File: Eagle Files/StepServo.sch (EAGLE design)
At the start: 8 parts, among them J2 1X2-3.5MM

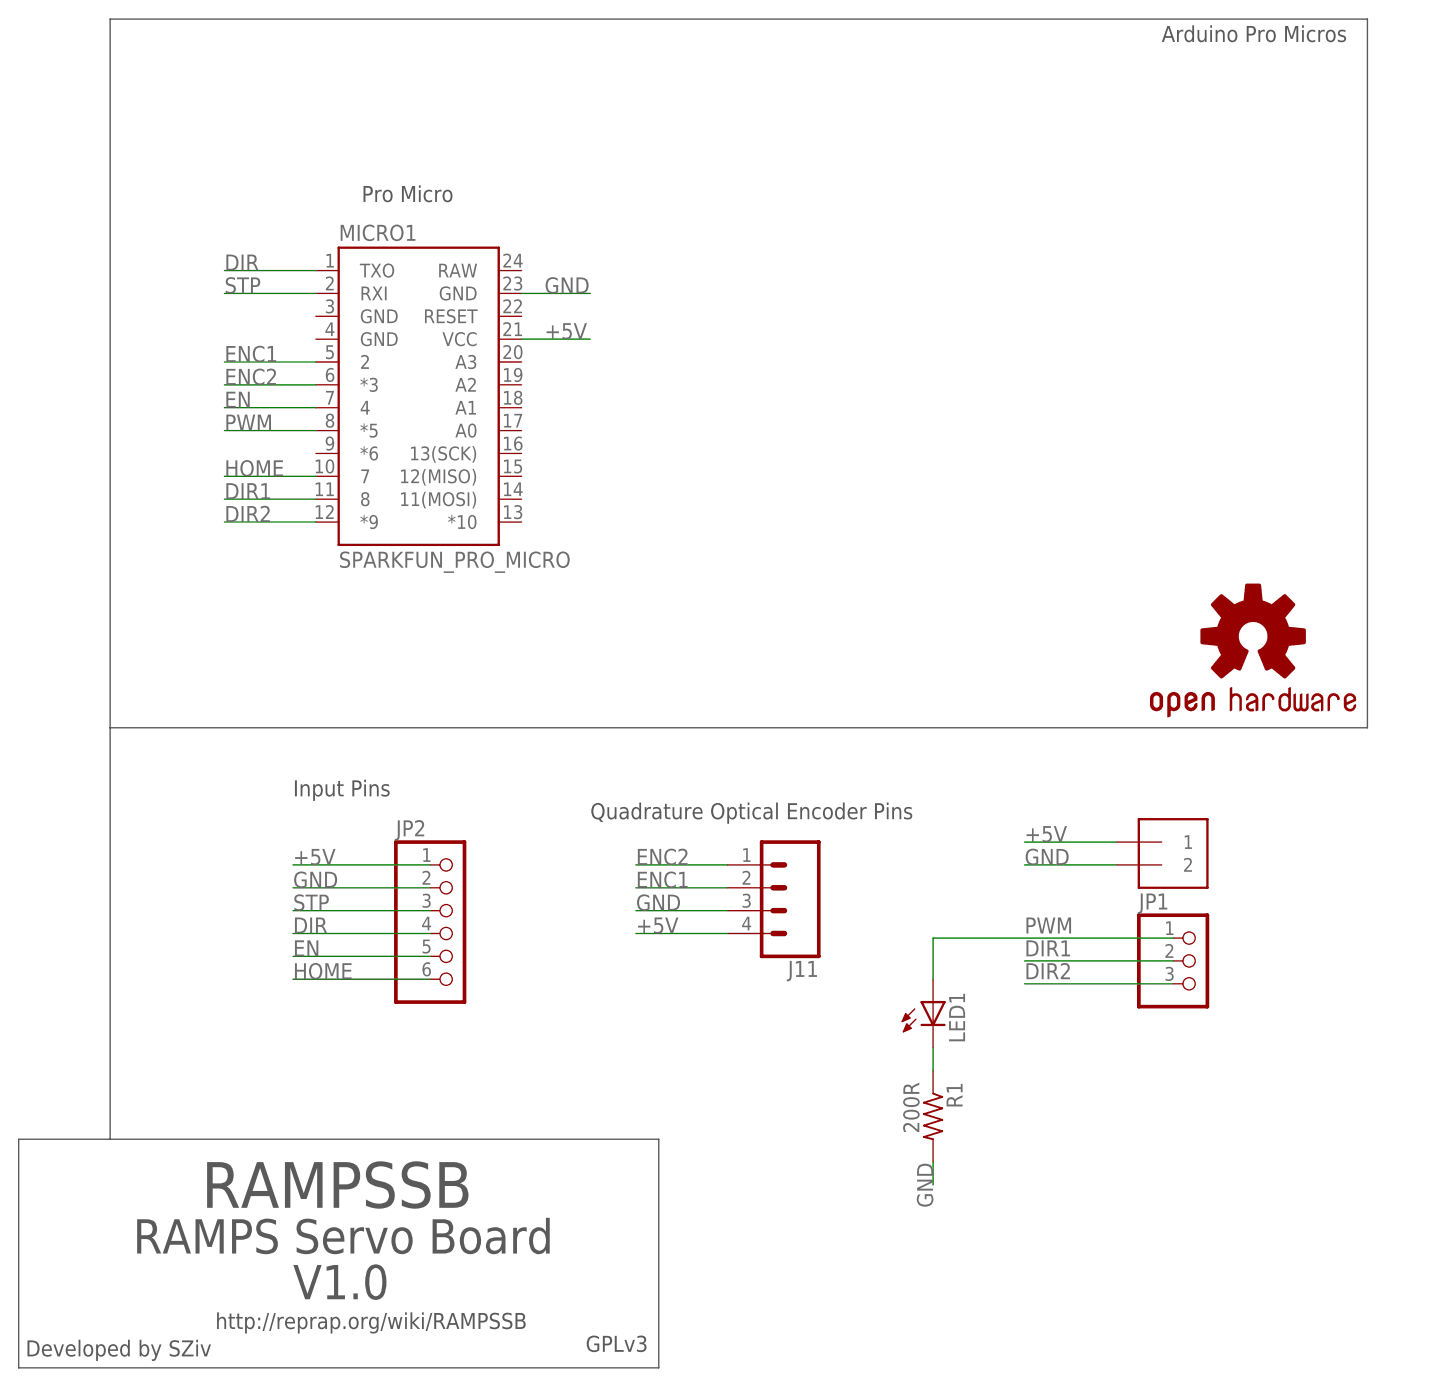
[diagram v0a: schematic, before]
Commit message: Fixed some bad markers on silkscreen, and cleaned up schematic
Fixed some bad markers on silkscreen, and cleaned up schematic
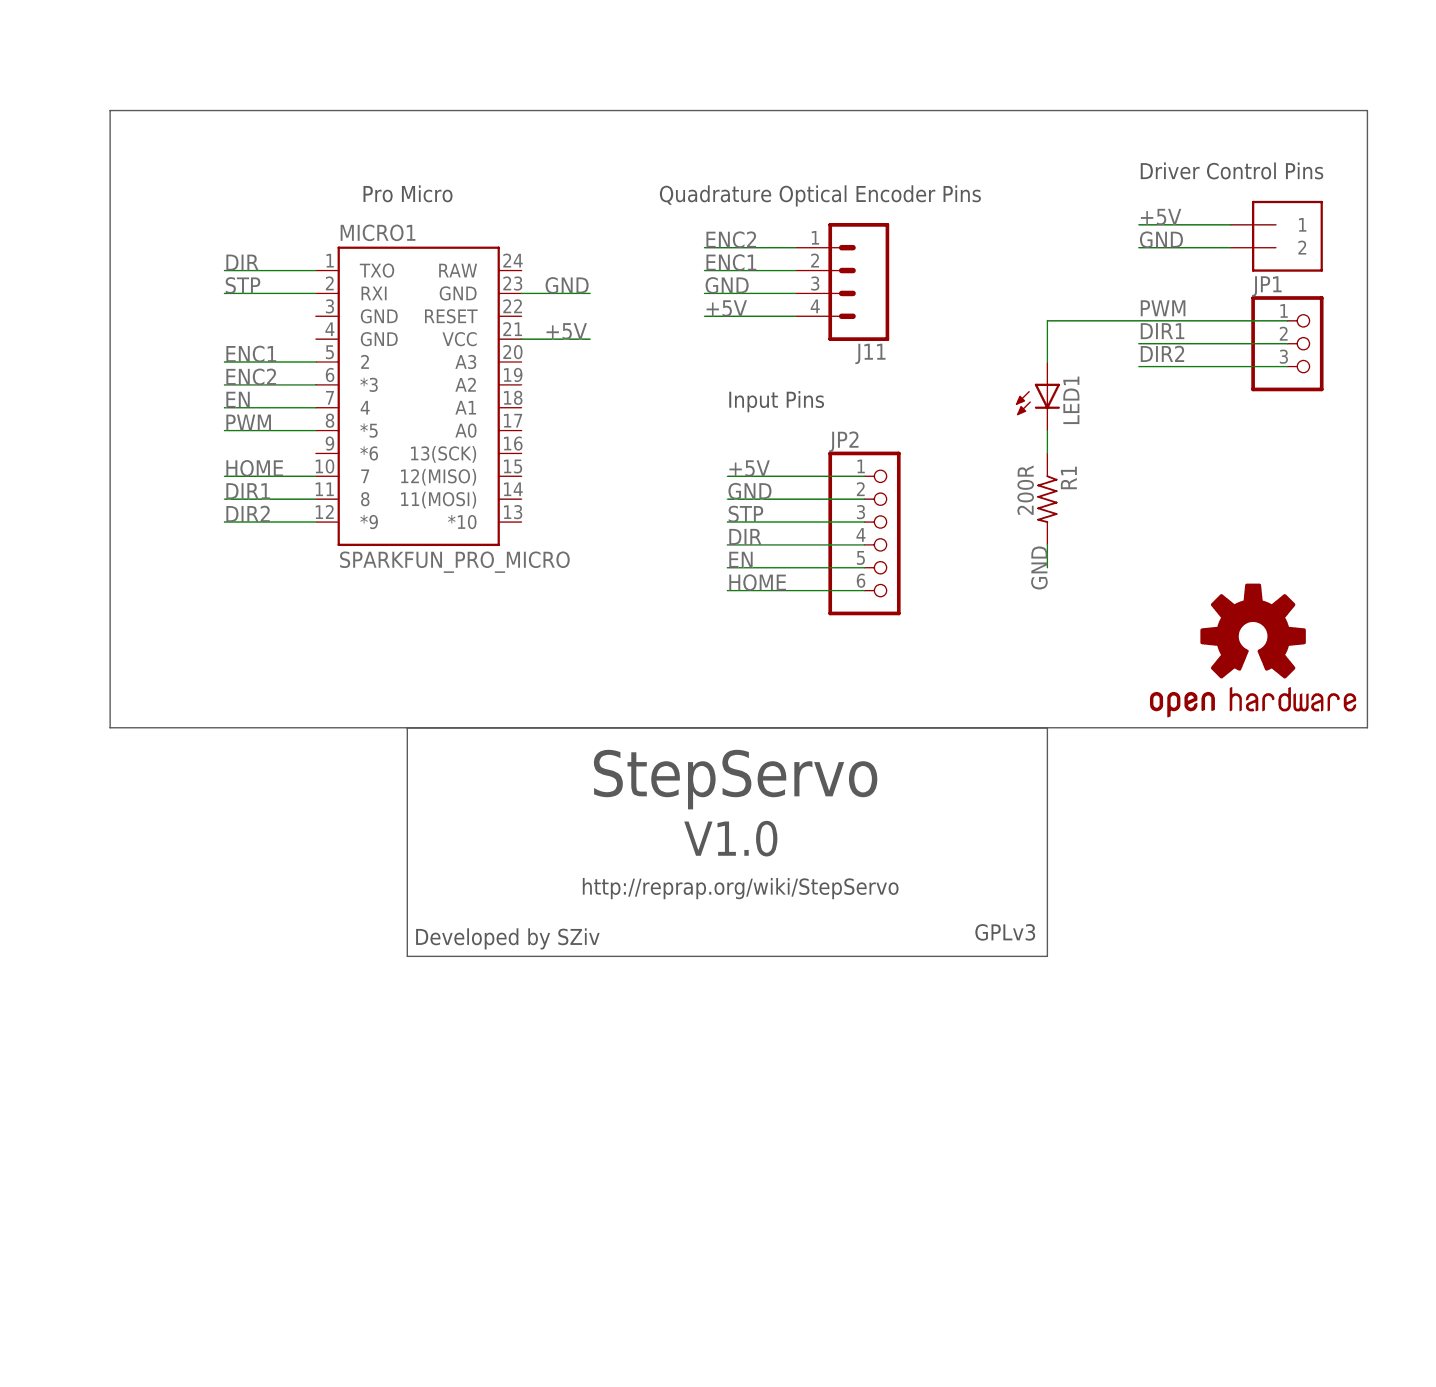
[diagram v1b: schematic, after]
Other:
- note added: "Driver Control Pins"
- note added: "StepServo"
- note added: "http://reprap.org/wiki/StepServo"
- note removed: "Arduino Pro Micros"
- note removed: "RAMPS Servo Board"
- note removed: "RAMPSSB"
- note removed: "http://reprap.org/wiki/RAMPSSB"
- moved on the sheet: J11, JP1, JP2, LED1, R1
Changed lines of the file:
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@@
 <plain>
 <text x="165.354" y="-80.01" size="3.81" layer="97"></text>
-<wire x1="27.94" y1="-12.7" x2="99.06" y2="-12.7" width="0.1524" layer="97"/>
-<wire x1="177.8" y1="58.42" x2="177.8" y2="137.16" width="0.1524" layer="97"/>
-<wire x1="177.8" y1="137.16" x2="38.1" y2="137.16" width="0.1524" layer="97"/>
-<wire x1="38.1" y1="137.16" x2="38.1" y2="58.42" width="0.1524" layer="97"/>
+<wire x1="71.12" y1="33.02" x2="142.24" y2="33.02" width="0.1524" layer="97"/>
+<wire x1="177.8" y1="58.42" x2="177.8" y2="127" width="0.1524" layer="97"/>
+<wire x1="177.8" y1="127" x2="38.1" y2="127" width="0.1524" layer="97"/>
+<wire x1="38.1" y1="127" x2="38.1" y2="58.42" width="0.1524" layer="97"/>
 <wire x1="38.1" y1="58.42" x2="177.8" y2="58.42" width="0.1524" layer="97"/>
-<wire x1="38.1" y1="58.42" x2="38.1" y2="12.7" width="0.1524" layer="97"/>
-<wire x1="38.1" y1="12.7" x2="99.06" y2="12.7" width="0.1524" layer="97"/>
-<wire x1="99.06" y1="12.7" x2="99.06" y2="-12.7" width="0.1524" layer="97"/>
-<wire x1="38.1" y1="12.7" x2="27.94" y2="12.7" width="0.1524" layer="97"/>
-<wire x1="27.94" y1="12.7" x2="27.94" y2="-12.7" width="0.1524" layer="97"/>
-<text x="91.44" y="48.26" size="1.778" layer="97">Quadrature Optical Encoder Pins</text>
-<text x="154.94" y="134.62" size="1.778" layer="97">Arduino Pro Micros</text>
-<text x="48.26" y="5.08" size="5.08" layer="97">RAMPSSB</text>
-<text x="40.64" y="0" size="3.81" layer="97">RAMPS Servo Board</text>
-<text x="58.42" y="-5.08" size="3.81" layer="97">V1.0</text>
-<text x="28.702" y="-11.43" size="1.778" layer="97">Developed by SZiv</text>
-<text x="90.932" y="-10.922" size="1.778" layer="97">GPLv3</text>
-<text x="49.784" y="-8.382" size="1.778" layer="97">http://reprap.org/wiki/RAMPSSB</text>
+<wire x1="71.12" y1="58.42" x2="142.24" y2="58.42" width="0.1524" layer="97"/>
+<wire x1="142.24" y1="58.42" x2="142.24" y2="33.02" width="0.1524" layer="97"/>
+<wire x1="71.12" y1="58.42" x2="71.12" y2="33.02" width="0.1524" layer="97"/>
+<text x="99.06" y="116.84" size="1.778" layer="97">Quadrature Optical Encoder Pins</text>
+<text x="91.44" y="50.8" size="5.08" layer="97">StepServo</text>
+<text x="101.854" y="44.196" size="3.81" layer="97">V1.0</text>
+<text x="71.882" y="34.29" size="1.778" layer="97">Developed by SZiv</text>
+<text x="134.112" y="34.798" size="1.778" layer="97">GPLv3</text>
+<text x="90.424" y="39.878" size="1.778" layer="97">http://reprap.org/wiki/StepServo</text>
 <text x="66.04" y="116.84" size="1.778" layer="97">Pro Micro</text>
-<text x="58.42" y="50.8" size="1.778" layer="97">Input Pins</text>
+<text x="106.68" y="93.98" size="1.778" layer="97">Input Pins</text>
+<text x="152.4" y="119.38" size="1.778" layer="97">Driver Control Pins</text>
 </plain>
 <instances>
-<instance part="J11" gate="G$1" x="111.76" y="40.64" rot="R180"/>
+<instance part="J11" gate="G$1" x="119.38" y="109.22" rot="R180"/>
 <instance part="MICRO1" gate="G$1" x="71.12" y="93.98"/>
 <instance part="LOGO1" gate="G$1" x="165.1" y="68.58"/>
-<instance part="LED1" gate="G$1" x="129.54" y="27.94"/>
-<instance part="R1" gate="G$1" x="129.54" y="15.24" rot="R270"/>
-<instance part="J2" gate="G$1" x="154.94" y="43.18"/>
-<instance part="JP2" gate="A" x="76.2" y="35.56"/>
-<instance part="JP1" gate="A" x="158.75" y="32.512"/>
+<instance part="LED1" gate="G$1" x="142.24" y="96.52"/>
+<instance part="R1" gate="G$1" x="142.24" y="83.82" rot="R270"/>
+<instance part="J2" gate="G$1" x="167.64" y="111.76"/>
+<instance part="JP2" gate="A" x="124.46" y="78.74"/>
+<instance part="JP1" gate="A" x="171.45" y="101.092"/>
 </instances>
 <busses>
@@
 <segment>
 <pinref part="J11" gate="G$1" pin="4"/>
-<wire x1="96.52" y1="35.56" x2="106.68" y2="35.56" width="0.1524" layer="91"/>
-<label x="96.52" y="35.56" size="1.778" layer="95"/>
+<wire x1="104.14" y1="104.14" x2="114.3" y2="104.14" width="0.1524" layer="91"/>
+<label x="104.14" y="104.14" size="1.778" layer="95"/>
 </segment>
 <segment>
@@
 <segment>
 <pinref part="JP2" gate="A" pin="1"/>
-<wire x1="73.66" y1="43.18" x2="58.42" y2="43.18" width="0.1524" layer="91"/>
-<label x="58.42" y="43.18" size="1.778" layer="95"/>
+<wire x1="121.92" y1="86.36" x2="106.68" y2="86.36" width="0.1524" layer="91"/>
+<label x="106.68" y="86.36" size="1.778" layer="95"/>
 </segment>
 <segment>
 <pinref part="J2" gate="G$1" pin="1"/>
-<wire x1="149.86" y1="45.72" x2="139.7" y2="45.72" width="0.1524" layer="91"/>
-<label x="139.7" y="45.72" size="1.778" layer="95"/>
+<wire x1="162.56" y1="114.3" x2="152.4" y2="114.3" width="0.1524" layer="91"/>
+<label x="152.4" y="114.3" size="1.778" layer="95"/>
 </segment>
 </net>
@@
 <segment>
 <pinref part="J11" gate="G$1" pin="3"/>
-<wire x1="96.52" y1="38.1" x2="106.68" y2="38.1" width="0.1524" layer="91"/>
-<label x="96.52" y="38.1" size="1.778" layer="95"/>
+<wire x1="104.14" y1="106.68" x2="114.3" y2="106.68" width="0.1524" layer="91"/>
+<label x="104.14" y="106.68" size="1.778" layer="95"/>
 </segment>
 <segment>
@@
 <segment>
 <pinref part="JP2" gate="A" pin="2"/>
-<wire x1="73.66" y1="40.64" x2="58.42" y2="40.64" width="0.1524" layer="91"/>
-<label x="58.42" y="40.64" size="1.778" layer="95"/>
+<wire x1="121.92" y1="83.82" x2="106.68" y2="83.82" width="0.1524" layer="91"/>
+<label x="106.68" y="83.82" size="1.778" layer="95"/>
 </segment>
 <segment>
 <pinref part="J2" gate="G$1" pin="2"/>
-<wire x1="149.86" y1="43.18" x2="139.7" y2="43.18" width="0.1524" layer="91"/>
-<label x="139.7" y="43.18" size="1.778" layer="95"/>
+<wire x1="162.56" y1="111.76" x2="152.4" y2="111.76" width="0.1524" layer="91"/>
+<label x="152.4" y="111.76" size="1.778" layer="95"/>
 </segment>
 <segment>
 <pinref part="R1" gate="G$1" pin="2"/>
-<wire x1="129.54" y1="10.16" x2="129.54" y2="7.62" width="0.1524" layer="91"/>
-<label x="129.54" y="5.08" size="1.778" layer="95" rot="R90"/>
+<wire x1="142.24" y1="78.74" x2="142.24" y2="76.2" width="0.1524" layer="91"/>
+<label x="142.24" y="73.66" size="1.778" layer="95" rot="R90"/>
 </segment>
 </net>
@@
 <segment>
 <pinref part="JP1" gate="A" pin="2"/>
-<wire x1="156.21" y1="32.512" x2="139.7" y2="32.512" width="0.1524" layer="91"/>
-<label x="139.7" y="33.02" size="1.778" layer="95"/>
+<wire x1="168.91" y1="101.092" x2="152.4" y2="101.092" width="0.1524" layer="91"/>
+<label x="152.4" y="101.6" size="1.778" layer="95"/>
 </segment>
 </net>
@@
 <segment>
 <pinref part="JP1" gate="A" pin="3"/>
-<wire x1="156.21" y1="29.972" x2="139.7" y2="29.972" width="0.1524" layer="91"/>
-<label x="139.7" y="30.48" size="1.778" layer="95"/>
+<wire x1="168.91" y1="98.552" x2="152.4" y2="98.552" width="0.1524" layer="91"/>
+<label x="152.4" y="99.06" size="1.778" layer="95"/>
 </segment>
 </net>
@@
 <segment>
 <pinref part="JP2" gate="A" pin="4"/>
-<wire x1="73.66" y1="35.56" x2="58.42" y2="35.56" width="0.1524" layer="91"/>
-<label x="58.42" y="35.56" size="1.778" layer="95"/>
+<wire x1="121.92" y1="78.74" x2="106.68" y2="78.74" width="0.1524" layer="91"/>
+<label x="106.68" y="78.74" size="1.778" layer="95"/>
 </segment>
 </net>
@@
 <segment>
 <pinref part="JP2" gate="A" pin="3"/>
-<wire x1="73.66" y1="38.1" x2="58.42" y2="38.1" width="0.1524" layer="91"/>
-<label x="58.42" y="38.1" size="1.778" layer="95"/>
+<wire x1="121.92" y1="81.28" x2="106.68" y2="81.28" width="0.1524" layer="91"/>
+<label x="106.68" y="81.28" size="1.778" layer="95"/>
 </segment>
 </net>
@@
 <segment>
 <pinref part="J11" gate="G$1" pin="2"/>
-<wire x1="106.68" y1="40.64" x2="96.52" y2="40.64" width="0.1524" layer="91"/>
-<label x="96.52" y="40.64" size="1.778" layer="95"/>
+<wire x1="114.3" y1="109.22" x2="104.14" y2="109.22" width="0.1524" layer="91"/>
+<label x="104.14" y="109.22" size="1.778" layer="95"/>
 </segment>
 </net>
@@
 <segment>
 <pinref part="J11" gate="G$1" pin="1"/>
-<wire x1="106.68" y1="43.18" x2="96.52" y2="43.18" width="0.1524" layer="91"/>
-<label x="96.52" y="43.18" size="1.778" layer="95"/>
+<wire x1="114.3" y1="111.76" x2="104.14" y2="111.76" width="0.1524" layer="91"/>
+<label x="104.14" y="111.76" size="1.778" layer="95"/>
 </segment>
 </net>
@@
 <segment>
 <pinref part="JP2" gate="A" pin="5"/>
-<wire x1="73.66" y1="33.02" x2="58.42" y2="33.02" width="0.1524" layer="91"/>
-<label x="58.42" y="33.02" size="1.778" layer="95"/>
+<wire x1="121.92" y1="76.2" x2="106.68" y2="76.2" width="0.1524" layer="91"/>
+<label x="106.68" y="76.2" size="1.778" layer="95"/>
 </segment>
 </net>
@@
 <segment>
 <pinref part="JP1" gate="A" pin="1"/>
-<wire x1="156.21" y1="35.052" x2="129.54" y2="35.052" width="0.1524" layer="91"/>
-<label x="139.7" y="35.56" size="1.778" layer="95"/>
+<wire x1="168.91" y1="103.632" x2="142.24" y2="103.632" width="0.1524" layer="91"/>
+<label x="152.4" y="104.14" size="1.778" layer="95"/>
 <pinref part="LED1" gate="G$1" pin="A"/>
-<wire x1="129.54" y1="35.052" x2="129.54" y2="30.48" width="0.1524" layer="91"/>
+<wire x1="142.24" y1="103.632" x2="142.24" y2="99.06" width="0.1524" layer="91"/>
 </segment>
 </net>
@@
 <segment>
 <pinref part="JP2" gate="A" pin="6"/>
-<wire x1="73.66" y1="30.48" x2="58.42" y2="30.48" width="0.1524" layer="91"/>
-<label x="58.42" y="30.48" size="1.778" layer="95"/>
+<wire x1="121.92" y1="73.66" x2="106.68" y2="73.66" width="0.1524" layer="91"/>
+<label x="106.68" y="73.66" size="1.778" layer="95"/>
 </segment>
 </net>
@@
 <pinref part="LED1" gate="G$1" pin="C"/>
 <pinref part="R1" gate="G$1" pin="1"/>
-<wire x1="129.54" y1="22.86" x2="129.54" y2="20.32" width="0.1524" layer="91"/>
+<wire x1="142.24" y1="91.44" x2="142.24" y2="88.9" width="0.1524" layer="91"/>
 </segment>
 </net>
